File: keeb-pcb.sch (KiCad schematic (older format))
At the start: 14 parts

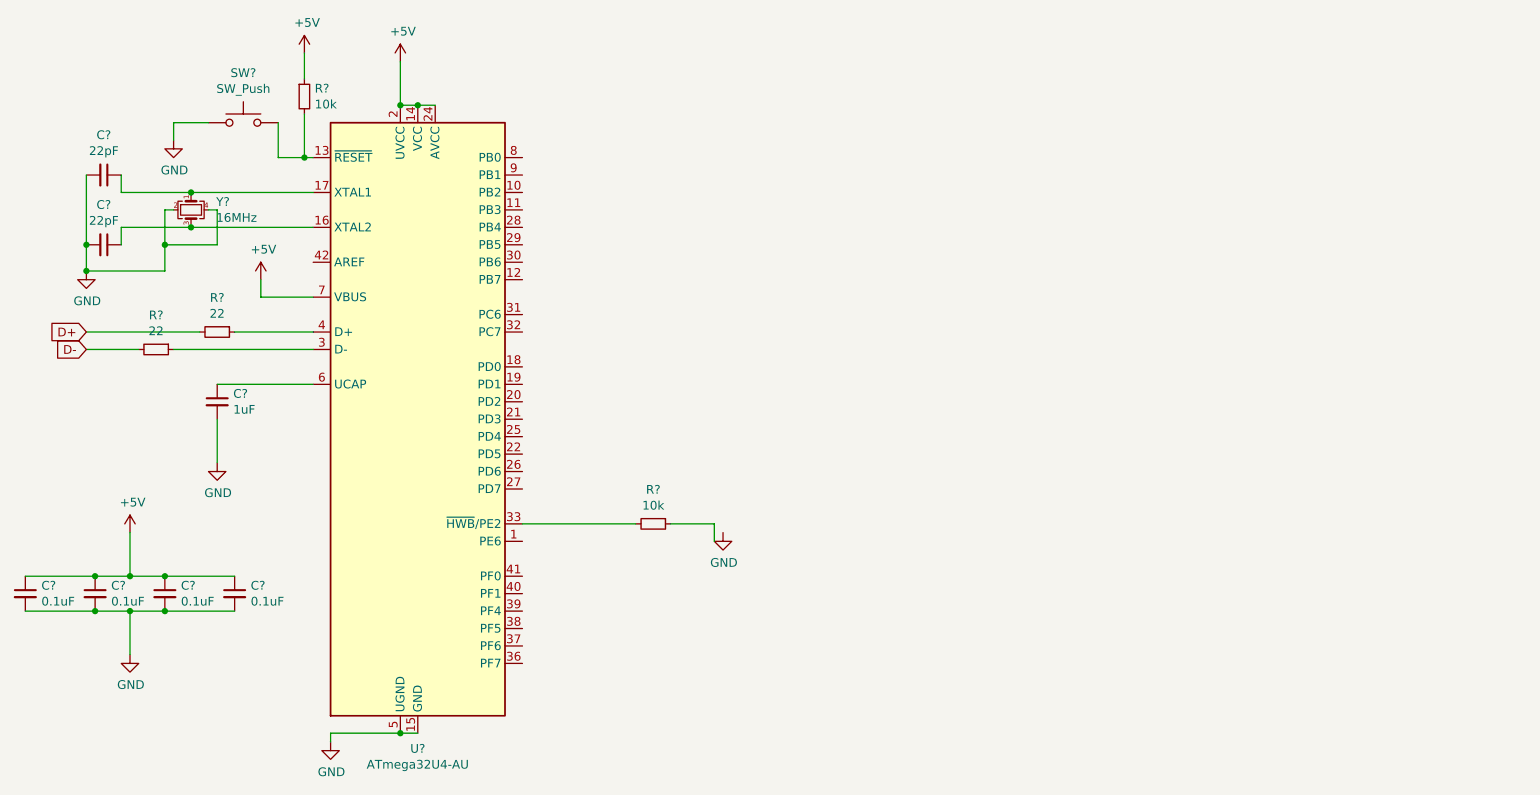
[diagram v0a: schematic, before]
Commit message: USB and Matrix Schematic
Added USB connector and Matrix Switches. PCB Guide Part 4
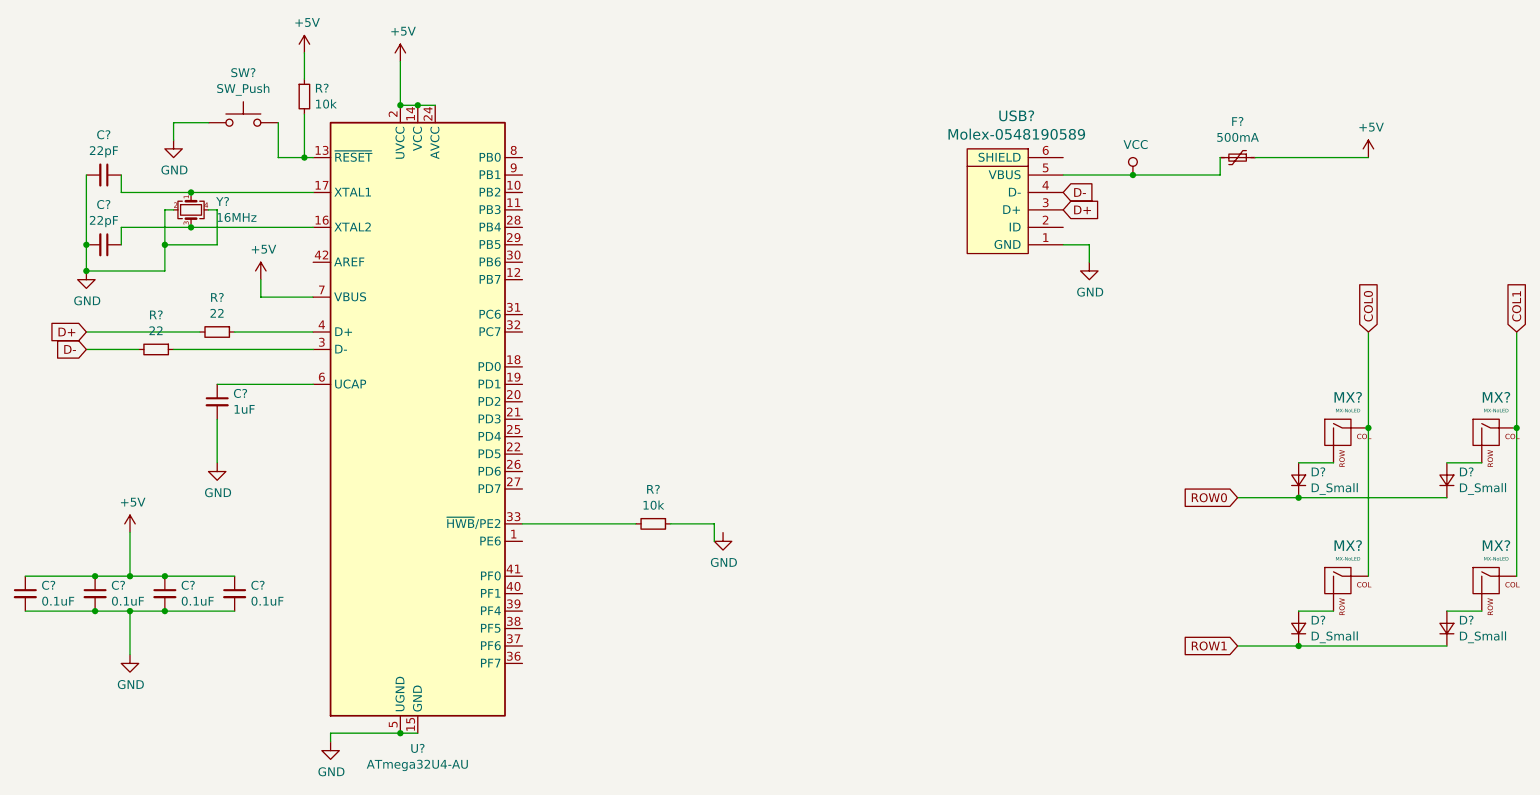
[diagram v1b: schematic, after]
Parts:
- added D? (x4): D_Small, symbol Device:D_Small
- added F?: 500mA, symbol Device:Polyfuse_Small
- added MX? (x4): MX-NoLED, symbol MX_Alps_Hybrid:MX-NoLED
- added USB?: Molex-0548190589, symbol random-keyboard-parts:Molex-0548190589
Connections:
- net +5V: now also F?.1
- net D+: now also USB?.3 (D+)
- net D-: now also USB?.4 (D-)
- net GND: now also USB?.1 (GND)
- new net: D?.2 (A), MX?.2 (ROW) (x4)
- new net COL0: MX?.1 (COL), MX?.1 (COL)
- new net COL1: MX?.1 (COL), MX?.1 (COL)
- new net ROW0: D?.1 (K), D?.1 (K)
- new net ROW1: D?.1 (K), D?.1 (K)
- new net VCC: F?.2, USB?.5 (VBUS)
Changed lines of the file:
@@
 Text GLabel 900  3600 0    50   Input ~ 0
 D-
+$Comp
+L random-keyboard-parts:Molex-0548190589 USB?
+U 1 1 5EBB7CB5
+P 6200 2800
+F 0 "USB?" V 6737 2767 60  0000 C CNN
+F 1 "Molex-0548190589" V 6631 2767 60  0000 C CNN
+F 2 "" H 6200 2800 60  0001 C CNN
+F 3 "" H 6200 2800 60  0001 C CNN
+	1    6200 2800
+	0    -1   -1   0
+$EndComp
+$Comp
+L Device:Polyfuse_Small F?
+U 1 1 5EBB993A
+P 7500 2500
+F 0 "F?" V 7295 2500 50  0000 C CNN
+F 1 "500mA" V 7386 2500 50  0000 C CNN
+F 2 "" H 7550 2300 50  0001 L CNN
+F 3 "~" H 7500 2500 50  0001 C CNN
+	1    7500 2500
+	0    1    1    0
+$EndComp
+Wire Wire Line
+	7400 2500 7400 2600
+Wire Wire Line
+	7400 2600 6900 2600
+$Comp
+L power:+5V #PWR?
+U 1 1 5EBC119E
+P 8250 2500
+F 0 "#PWR?" H 8250 2350 50  0001 C CNN
+F 1 "+5V" H 8265 2673 50  0000 C CNN
+F 2 "" H 8250 2500 50  0001 C CNN
+F 3 "" H 8250 2500 50  0001 C CNN
+	1    8250 2500
+	1    0    0    -1
+$EndComp
+Wire Wire Line
+	8250 2500 7600 2500
+$Comp
+L power:VCC #PWR?
+U 1 1 5EBC37C1
+P 6900 2600
+F 0 "#PWR?" H 6900 2450 50  0001 C CNN
+F 1 "VCC" H 6917 2773 50  0000 C CNN
+F 2 "" H 6900 2600 50  0001 C CNN
+F 3 "" H 6900 2600 50  0001 C CNN
+	1    6900 2600
+	1    0    0    -1
+$EndComp
+Connection ~ 6900 2600
+Wire Wire Line
+	6900 2600 6500 2600
+Text GLabel 6500 2700 2    50   Input ~ 0
+D-
+Text GLabel 6500 2800 2    50   Input ~ 0
+D+
+$Comp
+L power:GND #PWR?
+U 1 1 5EBC4B9B
+P 6650 3100
+F 0 "#PWR?" H 6650 2850 50  0001 C CNN
+F 1 "GND" H 6655 2927 50  0000 C CNN
+F 2 "" H 6650 3100 50  0001 C CNN
+F 3 "" H 6650 3100 50  0001 C CNN
+	1    6650 3100
+	1    0    0    -1
+$EndComp
+Wire Wire Line
+	6650 3100 6650 3000
+Wire Wire Line
+	6650 3000 6500 3000
+$Comp
+L MX_Alps_Hybrid:MX-NoLED MX?
+U 1 1 5EBC6A79
+P 8100 4100
+F 0 "MX?" H 8133 4323 60  0000 C CNN
+F 1 "MX-NoLED" H 8133 4249 20  0000 C CNN
+F 2 "" H 7475 4075 60  0001 C CNN
+F 3 "" H 7475 4075 60  0001 C CNN
+	1    8100 4100
+	1    0    0    -1
+$EndComp
+$Comp
+L Device:D_Small D?
+U 1 1 5EBCA196
+P 7850 4350
+F 0 "D?" V 7896 4282 50  0000 R CNN
+F 1 "D_Small" V 7805 4282 50  0000 R CNN
+F 2 "" V 7850 4350 50  0001 C CNN
+F 3 "~" V 7850 4350 50  0001 C CNN
+	1    7850 4350
+	0    -1   -1   0
+$EndComp
+Wire Wire Line
+	7850 4250 8050 4250
+$Comp
+L MX_Alps_Hybrid:MX-NoLED MX?
+U 1 1 5EBD1122
+P 8950 4100
+F 0 "MX?" H 8983 4323 60  0000 C CNN
+F 1 "MX-NoLED" H 8983 4249 20  0000 C CNN
+F 2 "" H 8325 4075 60  0001 C CNN
+F 3 "" H 8325 4075 60  0001 C CNN
+	1    8950 4100
+	1    0    0    -1
+$EndComp
+$Comp
+L MX_Alps_Hybrid:MX-NoLED MX?
+U 1 1 5EBD19ED
+P 8100 4950
+F 0 "MX?" H 8133 5173 60  0000 C CNN
+F 1 "MX-NoLED" H 8133 5099 20  0000 C CNN
+F 2 "" H 7475 4925 60  0001 C CNN
+F 3 "" H 7475 4925 60  0001 C CNN
+	1    8100 4950
+	1    0    0    -1
+$EndComp
+$Comp
+L MX_Alps_Hybrid:MX-NoLED MX?
+U 1 1 5EBD36C3
+P 8950 4950
+F 0 "MX?" H 8983 5173 60  0000 C CNN
+F 1 "MX-NoLED" H 8983 5099 20  0000 C CNN
+F 2 "" H 8325 4925 60  0001 C CNN
+F 3 "" H 8325 4925 60  0001 C CNN
+	1    8950 4950
+	1    0    0    -1
+$EndComp
+$Comp
+L Device:D_Small D?
+U 1 1 5EBD3FD4
+P 7850 5200
+F 0 "D?" V 7896 5132 50  0000 R CNN
+F 1 "D_Small" V 7805 5132 50  0000 R CNN
+F 2 "" V 7850 5200 50  0001 C CNN
+F 3 "~" V 7850 5200 50  0001 C CNN
+	1    7850 5200
+	0    -1   -1   0
+$EndComp
+$Comp
+L Device:D_Small D?
+U 1 1 5EBD4890
+P 8700 5200
+F 0 "D?" V 8746 5132 50  0000 R CNN
+F 1 "D_Small" V 8655 5132 50  0000 R CNN
+F 2 "" V 8700 5200 50  0001 C CNN
+F 3 "~" V 8700 5200 50  0001 C CNN
+	1    8700 5200
+	0    -1   -1   0
+$EndComp
+$Comp
+L Device:D_Small D?
+U 1 1 5EBD52AA
+P 8700 4350
+F 0 "D?" V 8746 4282 50  0000 R CNN
+F 1 "D_Small" V 8655 4282 50  0000 R CNN
+F 2 "" V 8700 4350 50  0001 C CNN
+F 3 "~" V 8700 4350 50  0001 C CNN
+	1    8700 4350
+	0    -1   -1   0
+$EndComp
+Wire Wire Line
+	8700 4250 8900 4250
+Wire Wire Line
+	7850 5100 8050 5100
+Wire Wire Line
+	8700 5100 8900 5100
+Wire Wire Line
+	8250 4900 8250 4050
+Connection ~ 8250 4050
+Wire Wire Line
+	8250 4050 8250 3500
+Wire Wire Line
+	9100 4900 9100 4050
+Connection ~ 9100 4050
+Wire Wire Line
+	9100 4050 9100 3500
+Wire Wire Line
+	8700 4450 7850 4450
+Connection ~ 7850 4450
+Wire Wire Line
+	7850 4450 7500 4450
+Wire Wire Line
+	8700 5300 7850 5300
+Connection ~ 7850 5300
+Wire Wire Line
+	7850 5300 7500 5300
+Text GLabel 8250 3500 1    50   Input ~ 0
+COL0
+Text GLabel 9100 3500 1    50   Input ~ 0
+COL1
+Text GLabel 7500 4450 0    50   Input ~ 0
+ROW0
+Text GLabel 7500 5300 0    50   Input ~ 0
+ROW1
 $EndSCHEMATC

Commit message: Footprints
Assigned Footprints to Schematic - PCB Guide Part 4
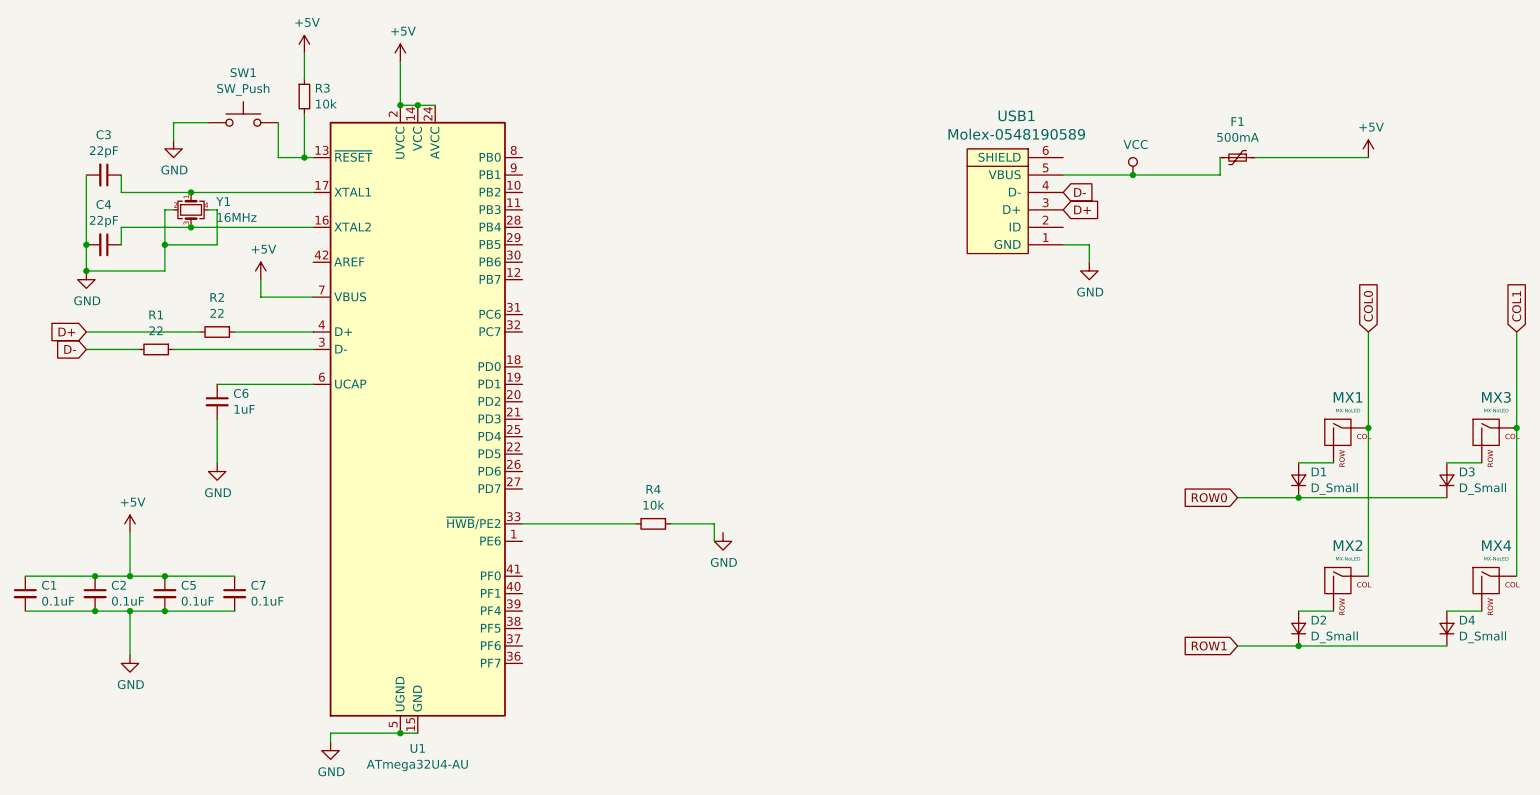
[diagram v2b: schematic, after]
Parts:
- C1, C2, C3, C4, C5, C6, C7: renamed from C?; footprint (none) -> Capacitor_SMD:C_0805_2012Metric
- D1, D2, D3, D4: renamed from D?; footprint (none) -> Diode_SMD:D_SOD-123
- F1: renamed from F?; footprint (none) -> Fuse:Fuse_1206_3216Metric
- MX1, MX2, MX3, MX4: renamed from MX?; footprint (none) -> MX_Alps_Hybrid:MX-1U
- R1, R2, R3, R4: renamed from R?; footprint (none) -> Resistor_SMD:R_0805_2012Metric
- SW1: renamed from SW?; footprint (none) -> random-keyboard-parts:SKQG-1155865
- USB1: renamed from USB?; footprint (none) -> random-keyboard-parts:Molex-0548190589
- Y1: renamed from Y?; footprint (none) -> Crystal:Crystal_SMD_3225-4Pin_3.2x2.5mm
- gave numbers to parts that had none: 1
